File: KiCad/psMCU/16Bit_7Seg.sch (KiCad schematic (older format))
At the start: 8 parts, among them U85 ATF16V8C, U86 ATF16V8C, U87 ATF16V8C, U88 ATF16V8C

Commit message: Updated values and footprints.
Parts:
- U85, U86, U87, U88: footprint (none) -> Package_SO:TSSOP-20_4.4x6.5mm_P0.65mm
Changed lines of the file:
@@
 $Descr A4 8268 11693 portrait
 encoding utf-8
-Sheet 21 110
+Sheet 18 110
 Title "psMCU"
 Date ""
@@
 F 0 "U85" H 3950 2300 50  0000 C CNN
 F 1 "ATF16V8C" H 4050 2200 50  0000 C CNN
-F 2 "" H 3350 1250 50  0001 C CNN
+F 2 "Package_SO:TSSOP-20_4.4x6.5mm_P0.65mm" H 3350 1250 50  0001 C CNN
 F 3 "" H 3350 1250 50  0001 C CNN
 	1    3800 1650
@@
 F 0 "U86" H 3950 4450 50  0000 C CNN
 F 1 "ATF16V8C" H 4050 4350 50  0000 C CNN
-F 2 "" H 3350 3400 50  0001 C CNN
+F 2 "Package_SO:TSSOP-20_4.4x6.5mm_P0.65mm" H 3350 3400 50  0001 C CNN
 F 3 "" H 3350 3400 50  0001 C CNN
 	1    3800 3800
@@
 F 0 "U87" H 3950 6650 50  0000 C CNN
 F 1 "ATF16V8C" H 4050 6550 50  0000 C CNN
-F 2 "" H 3350 5600 50  0001 C CNN
+F 2 "Package_SO:TSSOP-20_4.4x6.5mm_P0.65mm" H 3350 5600 50  0001 C CNN
 F 3 "" H 3350 5600 50  0001 C CNN
 	1    3800 6000
@@
 F 0 "U88" H 3950 8750 50  0000 C CNN
 F 1 "ATF16V8C" H 4050 8650 50  0000 C CNN
-F 2 "" H 3350 7700 50  0001 C CNN
+F 2 "Package_SO:TSSOP-20_4.4x6.5mm_P0.65mm" H 3350 7700 50  0001 C CNN
 F 3 "" H 3350 7700 50  0001 C CNN
 	1    3800 8100

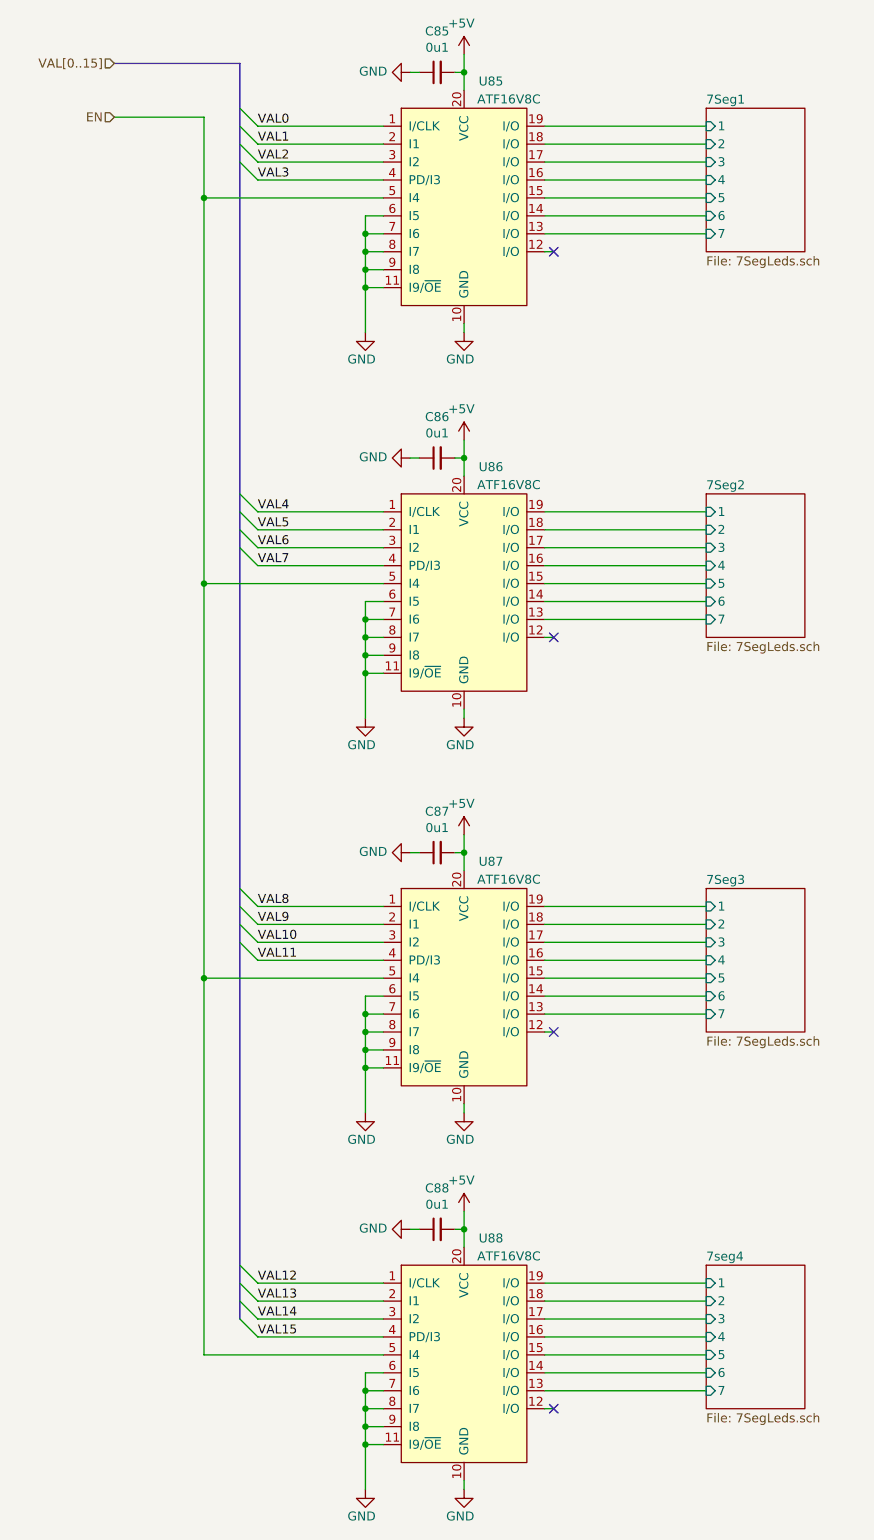
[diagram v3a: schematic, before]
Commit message: Reworked ref. location in schematic.
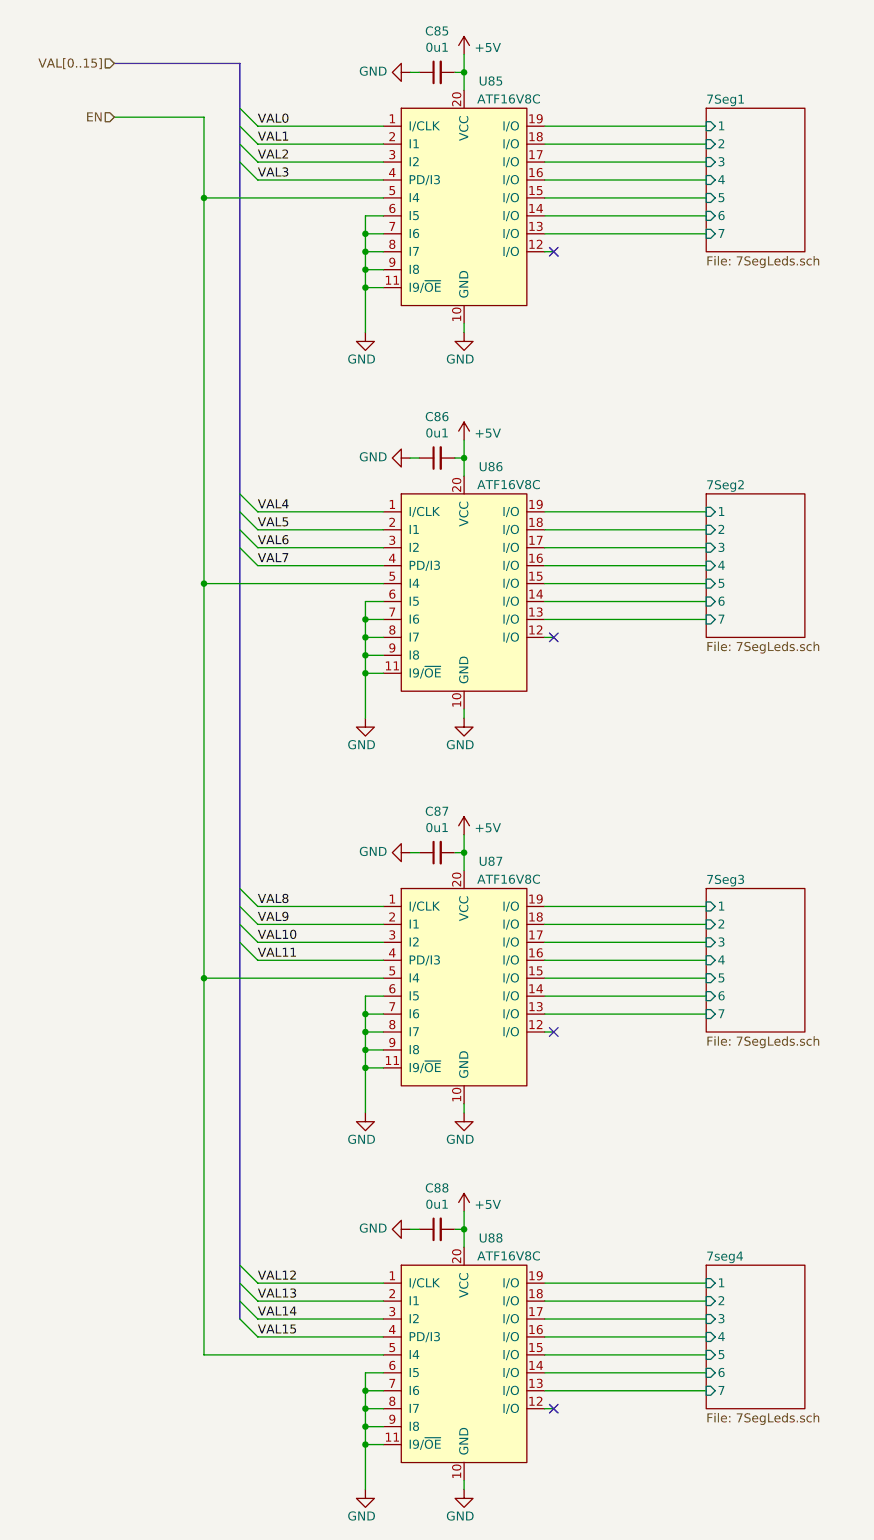
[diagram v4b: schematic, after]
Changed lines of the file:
@@
 AR Path="/5F18F3CA/6032BB0E/61AA9AB8" Ref="#PWR0336"  Part="1"
 F 0 "#PWR0336" H 3800 700 50  0001 C CNN
-F 1 "+5V" H 3815 1023 50  0000 C CNN
+F 1 "+5V" H 3742 887 50  0000 R CNN
 F 2 "" H 3800 850 50  0001 C CNN
 F 3 "" H 3800 850 50  0001 C CNN
@@
 AR Path="/5F18F3CA/6032BB0E/60486AA3" Ref="#PWR0338"  Part="1"
 F 0 "#PWR0338" H 3800 2850 50  0001 C CNN
-F 1 "+5V" H 3815 3173 50  0000 C CNN
+F 1 "+5V" H 3742 3037 50  0000 R CNN
 F 2 "" H 3800 3000 50  0001 C CNN
 F 3 "" H 3800 3000 50  0001 C CNN
@@
 AR Path="/5F18F3CA/6032BB0E/6049E3B6" Ref="#PWR0340"  Part="1"
 F 0 "#PWR0340" H 3800 5050 50  0001 C CNN
-F 1 "+5V" H 3815 5373 50  0000 C CNN
+F 1 "+5V" H 3742 5237 50  0000 R CNN
 F 2 "" H 3800 5200 50  0001 C CNN
 F 3 "" H 3800 5200 50  0001 C CNN
@@
 AR Path="/5F18F3CA/6032BB0E/603B3BC9" Ref="#PWR0342"  Part="1"
 F 0 "#PWR0342" H 3800 7150 50  0001 C CNN
-F 1 "+5V" H 3815 7473 50  0000 C CNN
+F 1 "+5V" H 3742 7337 50  0000 R CNN
 F 2 "" H 3800 7300 50  0001 C CNN
 F 3 "" H 3800 7300 50  0001 C CNN

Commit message: Finished Schematic Validation/Documentation
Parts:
- U85, U86, U87, U88: value ATF16V8C -> ATF16V8CZ-15XU
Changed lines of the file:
@@
 AR Path="/5F18F3CA/6032BB0E/60486A4C" Ref="U85"  Part="1"
 F 0 "U85" H 3950 2300 50  0000 C CNN
-F 1 "ATF16V8C" H 4050 2200 50  0000 C CNN
+F 1 "ATF16V8CZ-15XU" H 4200 2200 50  0000 C CNN
 F 2 "Package_SO:TSSOP-20_4.4x6.5mm_P0.65mm" H 3350 1250 50  0001 C CNN
 F 3 "" H 3350 1250 50  0001 C CNN
@@
 AR Path="/5F18F3CA/6032BB0E/61AA9ABB" Ref="U86"  Part="1"
 F 0 "U86" H 3950 4450 50  0000 C CNN
-F 1 "ATF16V8C" H 4050 4350 50  0000 C CNN
+F 1 "ATF16V8CZ-15XU" H 4200 4350 50  0000 C CNN
 F 2 "Package_SO:TSSOP-20_4.4x6.5mm_P0.65mm" H 3350 3400 50  0001 C CNN
 F 3 "" H 3350 3400 50  0001 C CNN
@@
 AR Path="/5F18F3CA/6032BB0E/61AA9AC1" Ref="U87"  Part="1"
 F 0 "U87" H 3950 6650 50  0000 C CNN
-F 1 "ATF16V8C" H 4050 6550 50  0000 C CNN
+F 1 "ATF16V8CZ-15XU" H 4200 6550 50  0000 C CNN
 F 2 "Package_SO:TSSOP-20_4.4x6.5mm_P0.65mm" H 3350 5600 50  0001 C CNN
 F 3 "" H 3350 5600 50  0001 C CNN
@@
 AR Path="/5F18F3CA/6032BB0E/603B3BB3" Ref="U88"  Part="1"
 F 0 "U88" H 3950 8750 50  0000 C CNN
-F 1 "ATF16V8C" H 4050 8650 50  0000 C CNN
+F 1 "ATF16V8CZ-15XU" H 4200 8650 50  0000 C CNN
 F 2 "Package_SO:TSSOP-20_4.4x6.5mm_P0.65mm" H 3350 7700 50  0001 C CNN
 F 3 "" H 3350 7700 50  0001 C CNN
